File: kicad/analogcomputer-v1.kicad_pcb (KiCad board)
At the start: 2 copper layers, 245.1 x 121.1 mm, 75 parts, among them U1 TL082

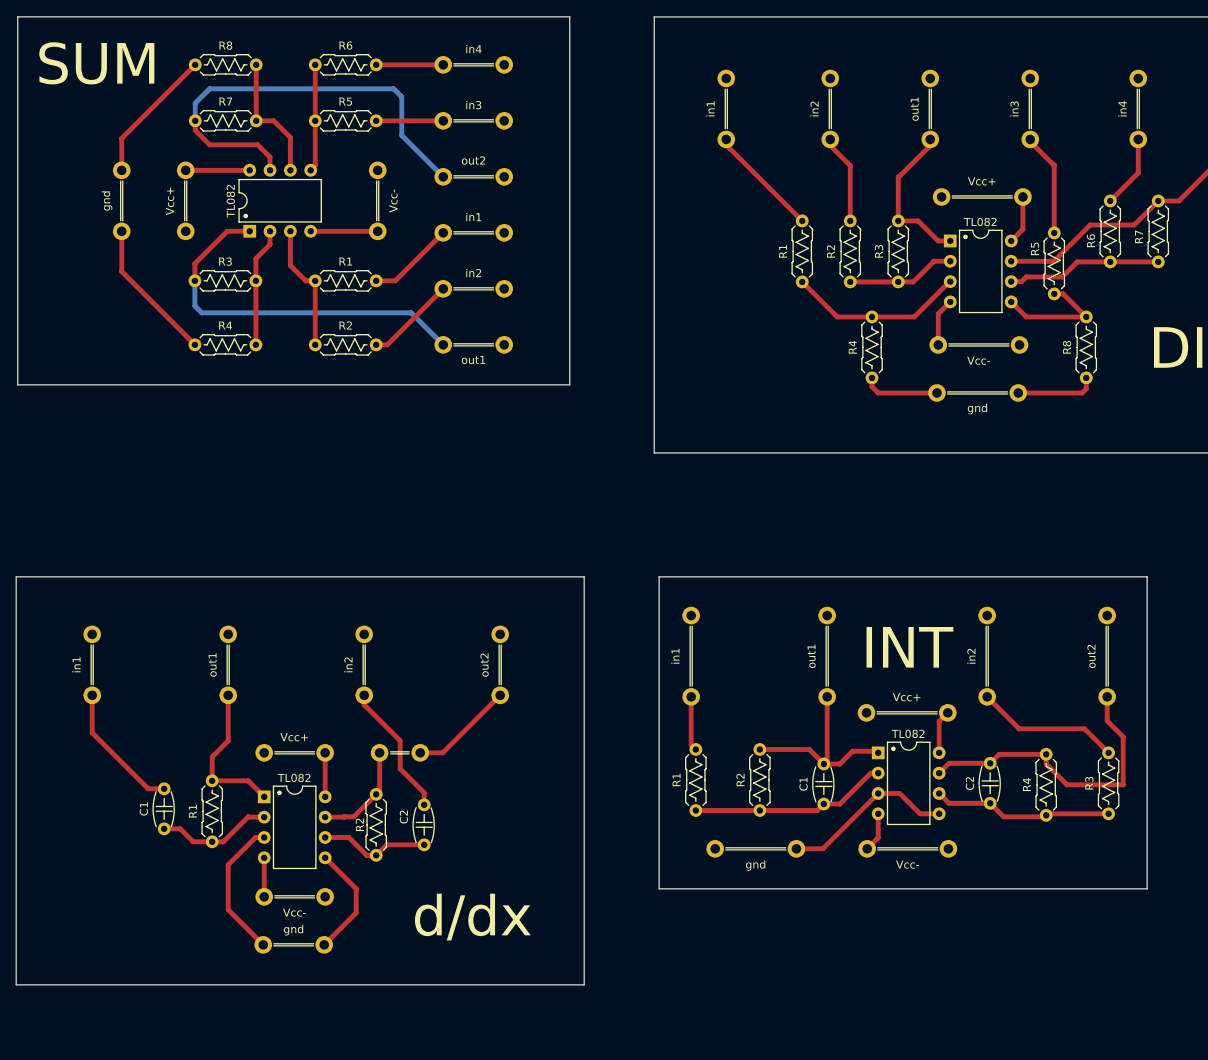
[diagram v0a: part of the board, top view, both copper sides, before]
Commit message: updated sum with larger output spacing
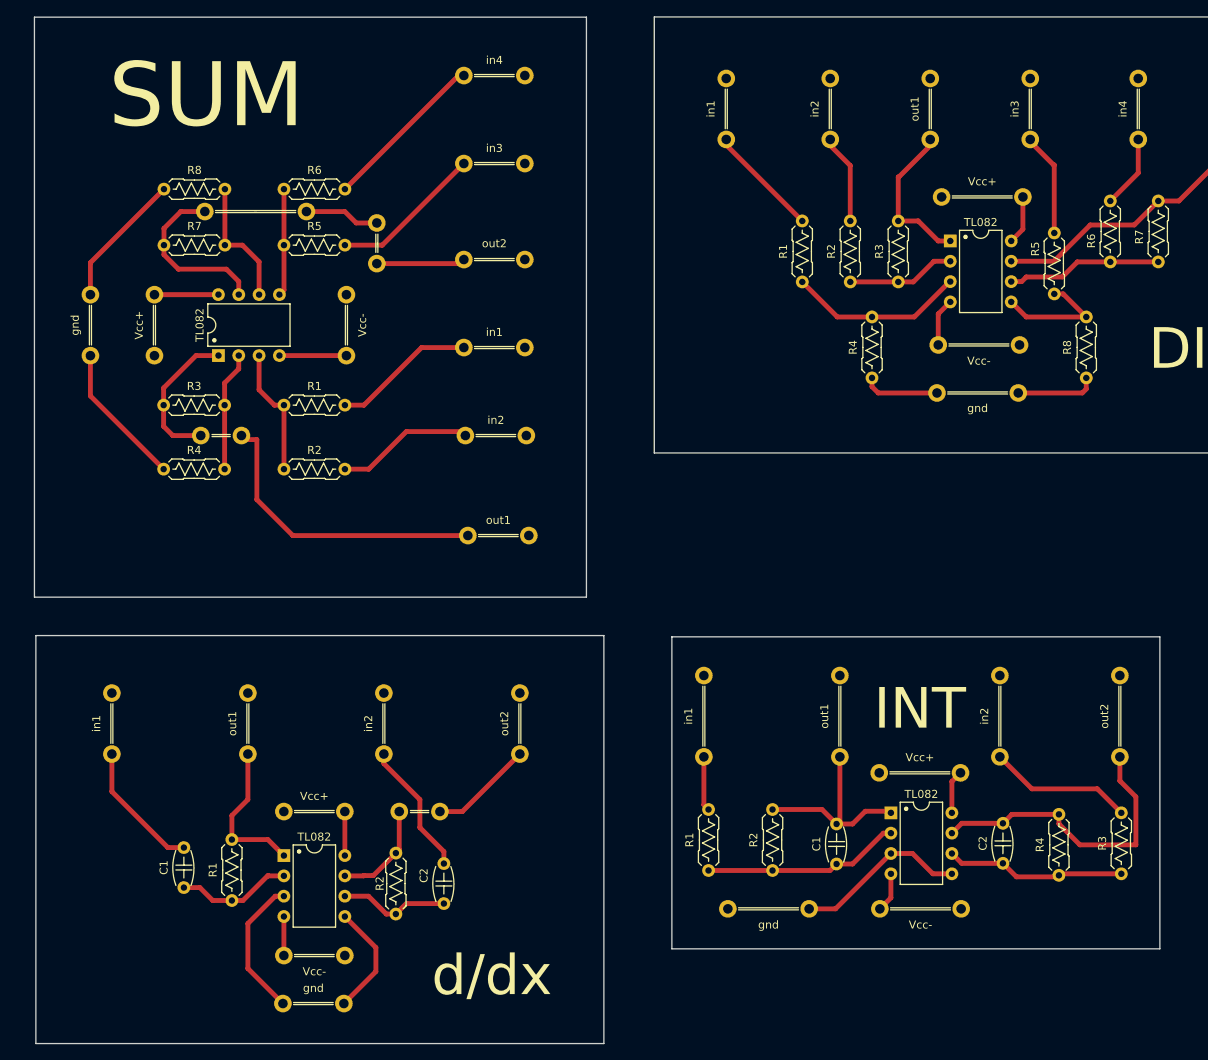
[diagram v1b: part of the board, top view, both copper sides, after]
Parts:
- added -: Jumper_P12.70mm_D1.2mm, PCM_Jumper_AKL:Jumper_P12.70mm_D1.2mm, F.Cu at (40.5, 41.5)
- added -: Jumper_P5.08mm_D1.2mm, PCM_Jumper_AKL:Jumper_P5.08mm_D1.2mm, F.Cu at (40.0, 69.5)
- added -: Jumper_P5.08mm_D1.2mm, PCM_Jumper_AKL:Jumper_P5.08mm_D1.2mm, F.Cu at (62.0, 48.0)
- R1, R2, R3, R4, R5, R6, R7, R8: footprint PCM_Resistor_THT_US_AKL:R_Axial_DIN0207_L6.3mm_D2.5mm_P7.62mm_Horizontal -> PCM_Resistor_THT_US_AKL_Double:R_Axial_DIN0207_L6.3mm_D2.5mm_P7.62mm_Horizontal
- moved out1 24.3 mm to (73.4, 82.0), turned to 0 degrees
- moved in2 18.5 mm to (73.1, 69.5)
- moved R1 16.0 mm to (50.4, 65.7)
- moved R2 16.0 mm to (50.4, 73.7)
- moved R3 16.0 mm to (35.4, 65.7)
- moved R4 16.0 mm to (35.4, 73.7)
- moved R5 16.0 mm to (50.4, 45.7)
- moved R6 16.0 mm to (50.4, 38.7)
- moved R7 16.0 mm to (35.4, 45.7)
- moved R8 16.0 mm to (35.4, 38.7)
- moved TL082 16.0 mm to (42.2, 59.5)
- moved Vcc+ 16.0 mm to (34.2, 59.5)
- moved Vcc- 16.0 mm to (58.2, 59.5)
- moved gnd 16.0 mm to (26.2, 59.5)
- moved in1 14.6 mm to (72.9, 58.5)
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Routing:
- net (no net): track 925.6 -> 958.1 mm
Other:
- board size 245.1 x 121.1 mm -> 242.8 x 128.4 mm

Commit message: updated differentiation circuit and spacing
Spacing of ins/outs, added input resistor to differentiation circuit.
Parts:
- removed the - at (69.9, 116.5)
- added R1: R_Axial_DIN0207_L6.3mm_D2.5mm_P7.62mm_Horizontal, PCM_Resistor_THT_US_AKL:R_Axial_DIN0207_L6.3mm_D2.5mm_P7.62mm_Horizontal, F.Cu at (193.0, 105.0)
- added R3: R_Axial_DIN0207_L6.3mm_D2.5mm_P7.62mm_Horizontal, PCM_Resistor_THT_US_AKL:R_Axial_DIN0207_L6.3mm_D2.5mm_P7.62mm_Horizontal, F.Cu at (226.0, 105.0)
- moved R2 156.6 mm to (199.5, 110.1)
- moved R4 156.6 mm to (220.0, 104.2)
- moved TL082 156.6 mm to (206.0, 104.5)
- moved Vcc+ 156.6 mm to (206.0, 99.0)
- moved Vcc- 156.6 mm to (206.0, 117.0)
- moved gnd 156.6 mm to (205.9, 123.0)
- moved in1 156.6 mm to (184.5, 91.8)
- moved in2 156.6 mm to (218.5, 91.8)
- moved out1 156.6 mm to (201.5, 91.8)
- moved out2 156.6 mm to (235.5, 91.8)
- moved C2 156.2 mm to (226.0, 114.0)
- moved C1 155.6 mm to (193.0, 114.0)
- moved C1 127.8 mm to (223.2, 48.5)
- moved C2 127.8 mm to (244.0, 48.4)
- moved R1 127.8 mm to (207.2, 49.3)
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- renumbered R1 to R2, R2 to R4
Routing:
- net (no net): track 958.1 -> 998.0 mm
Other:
- board size 242.8 x 128.4 mm -> 243.6 x 115 mm
